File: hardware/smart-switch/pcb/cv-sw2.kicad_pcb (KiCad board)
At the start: 2 copper layers, 88.5 x 100 mm, 44 parts, among them J1 2P 5.08mm, J2 3P 5.08mm, K1 SRD-05VDC-SL-C, K2 SRD-05VDC-SL-C, Q1 S8050, Q2 S8050, U1 ESP32-WROOM-32E (4MB), U2 AMS1117-3.3, U3 PC817, U4 PC817

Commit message: hardware: fix mains isolation barrier gaps, add load-controller PCB
Adds the 13th board (ultra-compact dual-channel load controller: ESP32-C3,
opto+relay channel, MOSFET PWM channel, USB-C, AP2112K LDO, USBLC6 ESD) and
regenerates all 12 existing boards, which were stale with respect to earlier
relay-pinout and LED-polarity fixes.

The substantive change is to the mains isolation barrier. It is a keepout band
the router must not cross, deliberately cut where a component straddles it
because there the isolation is provided by the part's package. Three linked
defects made those cuts unsafe, each only visible once the previous was fixed:

1. The cut removed the barrier across the full band width for the straddling
   part's whole height, while the ISO_BRIDGE area that excuses the gap covered
   only the part itself. The router used the leftover strip beside the part to
   bring +5V within 6.99 mm of AC_N against an 8.0 mm reinforced creepage rule.
2. Straddling parts can overlap in y, so cutting per part put one part's
   keepout on another part's pads. The exempt x-ranges are now unioned per
   strip by a sweep line.
3. The rule only relaxes for items insideArea('ISO_BRIDGE'). With the hole the
   same size as the area, a track could hug the hole's edge without being
   contained in it, so the rule fired anyway and the router had no way to know.
   The hole is now the part's pad bbox + 0.3 mm, strictly inside ISO_BRIDGE at
   the footprint bbox + 0.6 mm.

The tighter hole leaves mains nets less room to reach bridge pads, so some
boards report more unconnected items. That is deliberate: those are documented
hand-routing items, whereas a creepage violation is a safety defect.

Also fixed in the generator:
- _pad_shape() derived a pad's layers from PAD::GetLayer(), which returns F.Cu
  even for pads on B.Cu. Every back-side pad became a phantom obstacle on the
  front, blocking legal paths there while hiding the real one behind. Only
  IsOnLayer() is truthful.
- Castella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
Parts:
- moved TP2 55.3 mm to (160.7, 157.1)
- moved TP1 52.4 mm to (157.1, 154.1)
- moved D2 47.5 mm to (172.1, 148.4)
- moved R3 47.5 mm to (175.1, 151.5)
- moved R4 47.5 mm to (179.5, 151.5)
- moved R6 47.5 mm to (156.6, 152.5)
- moved C2 47.5 mm to (165.0, 145.9)
- moved C3 47.5 mm to (152.9, 136.8)
- moved C4 47.5 mm to (157.4, 136.8)
- moved C5 47.5 mm to (162.8, 142.7)
- moved C6 47.5 mm to (167.3, 142.7)
- moved JP 47.5 mm to (153.0, 149.2)
- moved LED0 47.5 mm to (157.0, 149.6)
- moved R5 47.5 mm to (183.2, 152.2)
- moved R9 47.5 mm to (161.0, 155.5)
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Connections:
- K1 pad 2: RELAY1_SW -> +5V
- K1 pad 3: +5V -> RELAY1_SW
- K1 pad 4: RELAY1_COIL -> N$K1.4
- K1 pad 5: N$K1.5 -> RELAY1_COIL
- K2 pad 2: RELAY2_SW -> +5V
- K2 pad 3: +5V -> RELAY2_SW
- K2 pad 4: RELAY2_COIL -> N$K2.4
- K2 pad 5: N$K2.5 -> RELAY2_COIL
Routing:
- net AC_N: track 123.9 -> 0.00 mm
- net RELAY2_SW: track 74.0 -> 0.00 mm
- net AC_L_FUSED: track 101.9 -> 39.7 mm
- net +5V: track 176.6 -> 216.7 mm, vias 0 -> 1
- net RELAY1_SW: track 28.0 -> 0.00 mm
- net UART_TX: track 50.6 -> 74.9 mm
- net UART_RX: track 43.4 -> 64.1 mm, vias 1 -> 2
- net +3V3: track 157.7 -> 138.7 mm, vias 1 -> 6
- net EN: track 37.0 -> 55.4 mm
- net RELAY1_OPT: track 30.6 -> 14.4 mm
- net RELAY2: track 55.6 -> 39.8 mm, vias 3 -> 1
- net RELAY1_COIL: track 77.9 -> 89.4 mm, vias 1 -> 0
- net RELAY2_COIL: track 87.1 -> 76.3 mm, vias 3 -> 1
- net TOUCH1__T0: track 40.0 -> 35.7 mm
- net GND: track 26.3 -> 29.5 mm, vias 235 -> 240
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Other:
- outline, holes or cut-outs redrawn
- board text removed: "!! MAINS !!"

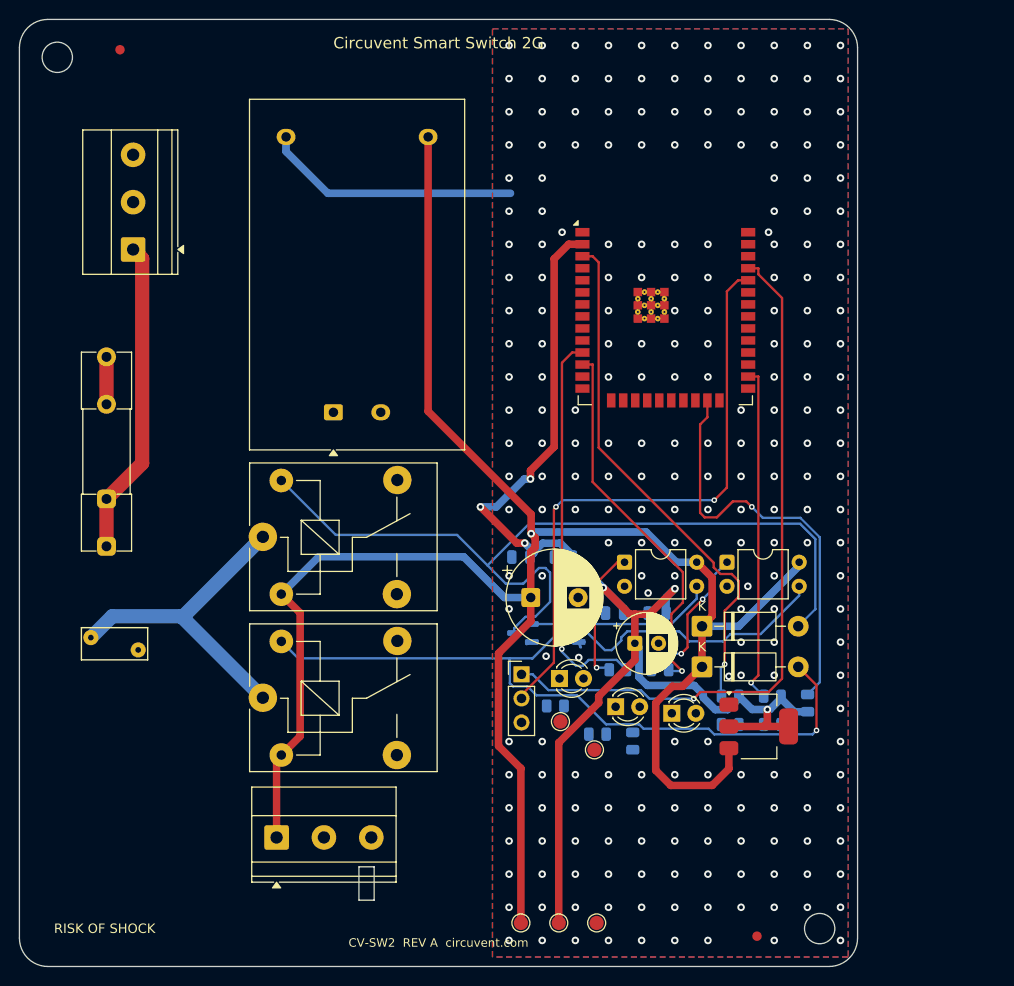
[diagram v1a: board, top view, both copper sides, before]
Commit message: Release 1.10.0, and stop shipping permissions the app never uses
Cut 1.10.0 (versionCode 12) and built it: AAB 38 MB, APK 83 MB, signed with the
upload key, JS bundle embedded.

Checking the generated manifest before writing the Play listing turned up
permissions no one had asked for. Every one of them is printed on the store page
for users to read before they install:

  RECORD_AUDIO          expo-camera asks for the microphone so video can be
                        recorded with sound. This app only ever puts the camera
                        in barcode mode to read a QR label, and expo-speech is
                        output-only - it speaks, it does not listen. Left in,
                        Play lists "Microphone" against a home-control app,
                        which is alarming, unexplainable and untrue.
  SYSTEM_ALERT_WINDOW   React Native's development overlay, useless in a release
                        build and shown to users as "Display over other apps".
  READ/WRITE_EXTERNAL_STORAGE
                        Legacy storage access nothing here touches.

Stripped via android.blockedPermissions. That emits tools:node="remove", which
is a merge instruction rather than a guarantee, so it was checked against the
finished artifact with aapt2 rather than the source manifest - all four are
absent from the APK.

NEARBY_WIFI_DEVICES now carries neverForLocation. Android otherwise treats it as
location-capable, because knowing which networks are in range is enough to place
someone, and Play's data safety review treats it the same way. The app uses it
only to join a new device's setup hotspot. That flag is a promise, so the plugin
says plainly that it has to come off if scan results are ever used positionally.

What is left is defensible: location for Wi-Fi onboarding (Android requires it),
camera for the QR label, nearby-devices flagged as non-positional.

Added mobile/store/listing with the text Play asks for - title, short and full
descriptions, and what'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
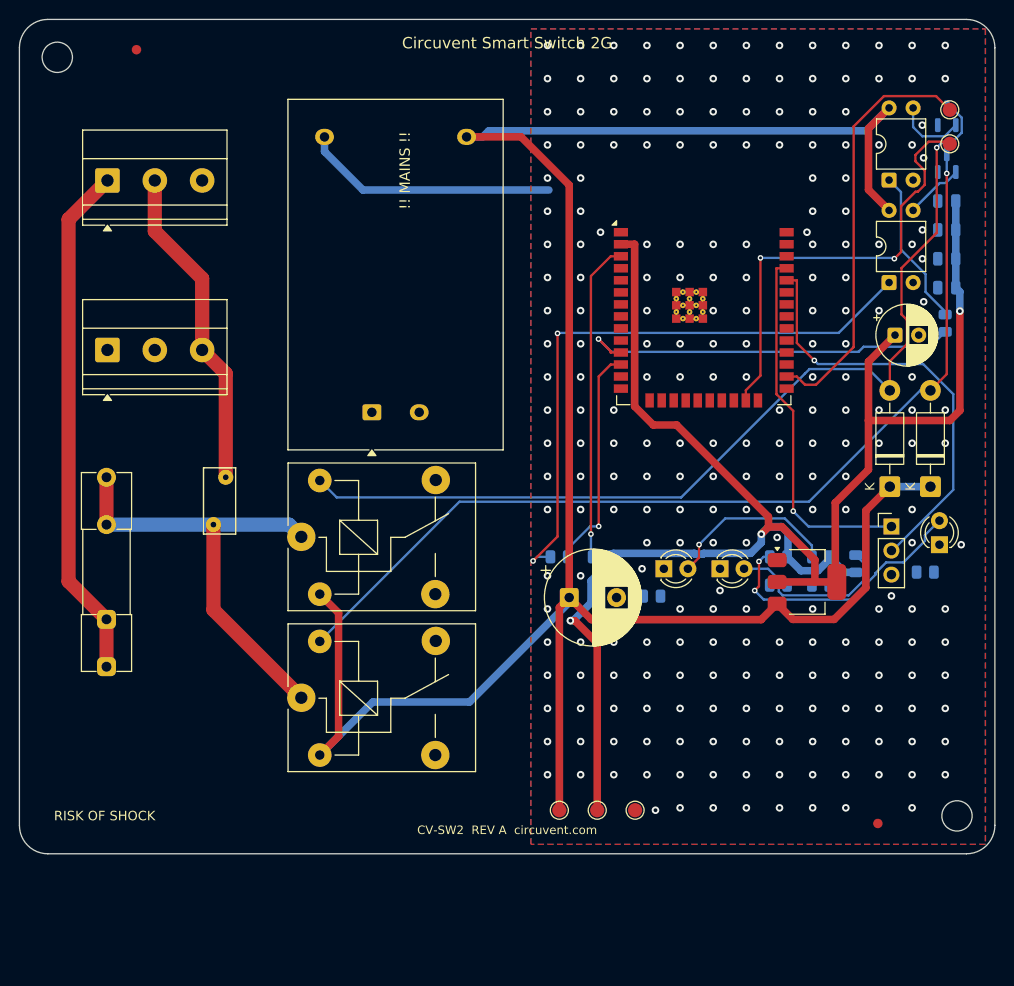
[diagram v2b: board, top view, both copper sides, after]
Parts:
- moved TP1 76.6 mm to (198.2, 89.5)
- moved TP2 74.2 mm to (198.2, 93.1)
- moved Q1 70.6 mm to (197.9, 90.2), turned to 90 degrees
- moved Q2 63.6 mm to (197.9, 95.2), turned to 90 degrees
- moved C3 58.6 mm to (197.9, 99.2)
- moved J2 54.5 mm to (109.3, 114.9)
- moved C4 53.2 mm to (197.9, 102.2)
- moved C5 51.3 mm to (197.9, 105.3)
- moved R1 50.3 mm to (197.8, 112.1), turned to 90 degrees
- moved U3 49.1 mm to (191.8, 97.0), turned to 90 degrees
- moved C6 46.0 mm to (197.9, 108.3)
- moved C2 42.6 mm to (192.5, 113.3)
- moved LED0 42.5 mm to (197.1, 135.5), turned to 90 degrees
- moved JP 42.1 mm to (192.1, 133.5)
- moved R6 35.1 mm to (188.3, 137.5), turned to 90 degrees
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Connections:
- J1 pad 3: RELAY2_SW -> PE
- J2 pad 1: +5V -> RELAY1_SW
- J2 pad 2: RELAY1_SW -> RELAY2_SW
- LED0 pad 1: N$LED0.1 -> GND
- LED0 pad 2: N$LED0.2 -> LED0_A
- LED1 pad 1: N$LED1.1 -> GND
- LED1 pad 2: N$LED1.2 -> LED1_A
- LED2 pad 1: N$LED2.1 -> GND
- LED2 pad 2: N$LED2.2 -> LED2_A
- R4 pad 2: TOUCH1__T0 -> LED0_A
- R5 pad 2: TOUCH2__T3 -> LED1_A
- R6 pad 1: N$R6.1 -> +3V3
- R6 pad 2: N$R6.2 -> LED2_A
- TP1 pad 1: N$TP1.1 -> TOUCH1__T0
- TP2 pad 1: N$TP2.1 -> TOUCH2__T3
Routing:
- net RELAY2_OPT: track 15.5 -> 64.3 mm
- net +3V3: track 138.7 -> 178.7 mm, vias 6 -> 3
- net UART_TX: track 74.9 -> 38.5 mm
- net AC_N: track 0.00 -> 34.4 mm
- net LED0_A: track 0.00 -> 28.4 mm, vias 0 -> 2
- net RELAY2_COIL: track 76.3 -> 101.1 mm
- net +5V: track 216.7 -> 241.1 mm, vias 1 -> 0
- net RELAY2_DRV: track 28.8 -> 6.28 mm
- net EN: track 55.4 -> 33.7 mm
- net AC_L: track 33.3 -> 54.7 mm
- net LED2_A: track 0.00 -> 18.5 mm
- net LED1_A: track 0.00 -> 18.5 mm, vias 0 -> 1
- net UART_RX: track 64.1 -> 45.7 mm, vias 2 -> 1
- net RELAY2: track 39.8 -> 23.8 mm
- net RELAY1_COIL: track 89.4 -> 102.5 mm, vias 0 -> 1
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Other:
- board size 88.5 x 100 mm -> 103 x 88.1 mm
- board text added: "!! MAINS !!"

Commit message: hardware: in-house 230VAC to 5V/3V3 isolated flyback to replace the HLK module
Twelve boards buy a Hi-Link HLK-PM03 and then spend an AMS1117 getting 3.3 V
out of it. This adds psu-5v3v3: a TNY274 flyback with opto/TL431 feedback that
produces both rails, so the host board drops its LDO and we stop depending on
one vendor for the part that makes everything else work.

New in the generator:

- hardware/lib/Circuvent.pretty, a repo-local footprint library, because KiCad
  ships no flyback bobbin and no safety-capacitor land. load_fp() prefers it
  over the KiCad install so a clean checkout rebuilds. The footprints are
  generated by make_lib.py, where every dimension is a named constant - the
  EE13 bobbin is a de facto standard rather than a controlled one, so that
  file is where you reconcile it with whoever winds the transformer.
- build_netlist_psu(), because a PSU has no MCU and the existing builder is
  organised around one.
- An HVDC netclass. Marking the whole primary as MAINS is correct about the
  hazard and wrong about the current: it forced 1.5 mm track and 2.0 mm
  clearance onto the BYPASS decoupling, and 33 of 33 primary nets failed to
  route. HVDC keeps a mains-grade gap to SELV and a sane one to itself.
- That split then broke reinforced_mains_to_selv, which excluded only MAINS
  and so began demanding 8 mm between AC_N and HV+ - two nets on the same side
  of the barrier, inside the same island. The two hazardous classes are now
  exempt from each other and both 8 mm from everything else.

Review found three defects in my own RCD clamp before it was committed: the
catch diode returned to the rail instead of catching at the drain, leaving the
leakage spike nowhere to go; the two snubber resistors were wired in parallel,
which halves the resistance instead of sharing the 325 V; and a decoupling cap
was orphaned.

The board is NOT fabricable as generated and the file says so. Thirteen
clearance errors remain, all primary copper against the optocoupler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
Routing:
- net +5V: track 241.1 -> 0.00 mm
- net +3V3: track 178.7 -> 6.30 mm, vias 3 -> 0
- net RELAY1_COIL: track 102.5 -> 0.00 mm, vias 1 -> 0
- net RELAY2_COIL: track 101.1 -> 0.00 mm, vias 1 -> 0
- net RELAY2_OPT: track 64.3 -> 0.00 mm, vias 2 -> 0
- net AC_L: track 54.7 -> 5.00 mm
- net TOUCH2__T3: track 47.0 -> 0.00 mm, vias 2 -> 0
- net UART_RX: track 45.7 -> 0.00 mm, vias 1 -> 0
- net TOUCH1__T0: track 44.5 -> 0.00 mm
- net AC_L_FUSED: track 48.2 -> 5.00 mm
- net RELAY1: track 41.1 -> 0.00 mm, vias 1 -> 0
- net UART_TX: track 38.5 -> 0.00 mm, vias 1 -> 0
- net AC_N: track 34.4 -> 0.00 mm
- net EN: track 33.7 -> 0.00 mm, vias 1 -> 0
- net LED0_A: track 28.4 -> 0.00 mm, vias 2 -> 0
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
